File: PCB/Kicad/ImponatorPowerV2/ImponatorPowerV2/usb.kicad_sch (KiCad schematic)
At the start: 10 parts, among them J1 USB type-c, U10 AO3401A, U4 ACS37041

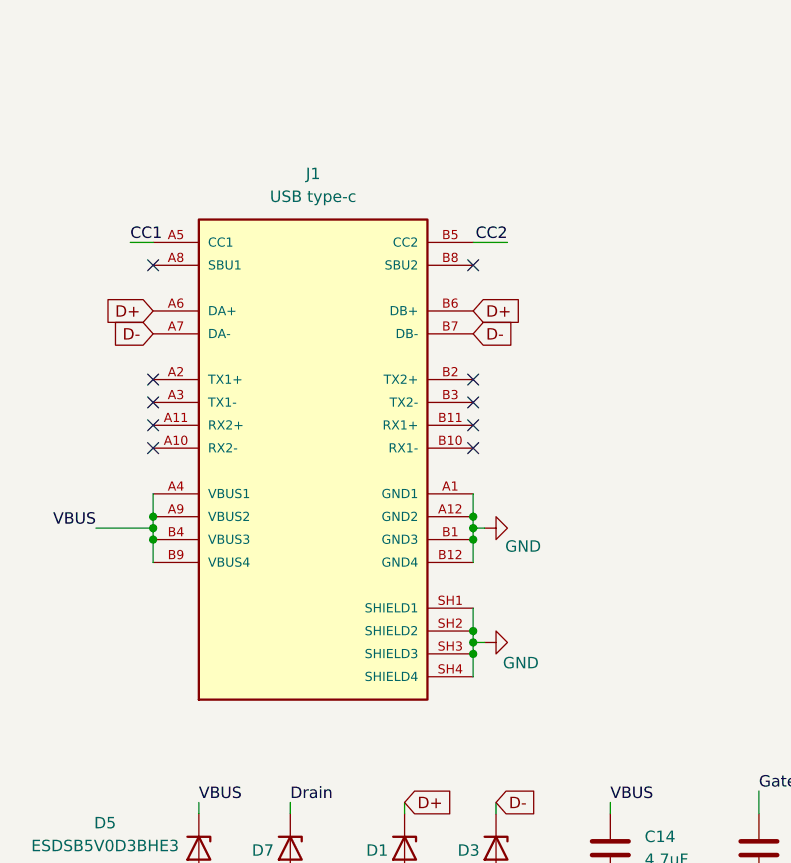
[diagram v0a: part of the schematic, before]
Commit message: PCB routed, not ready for production
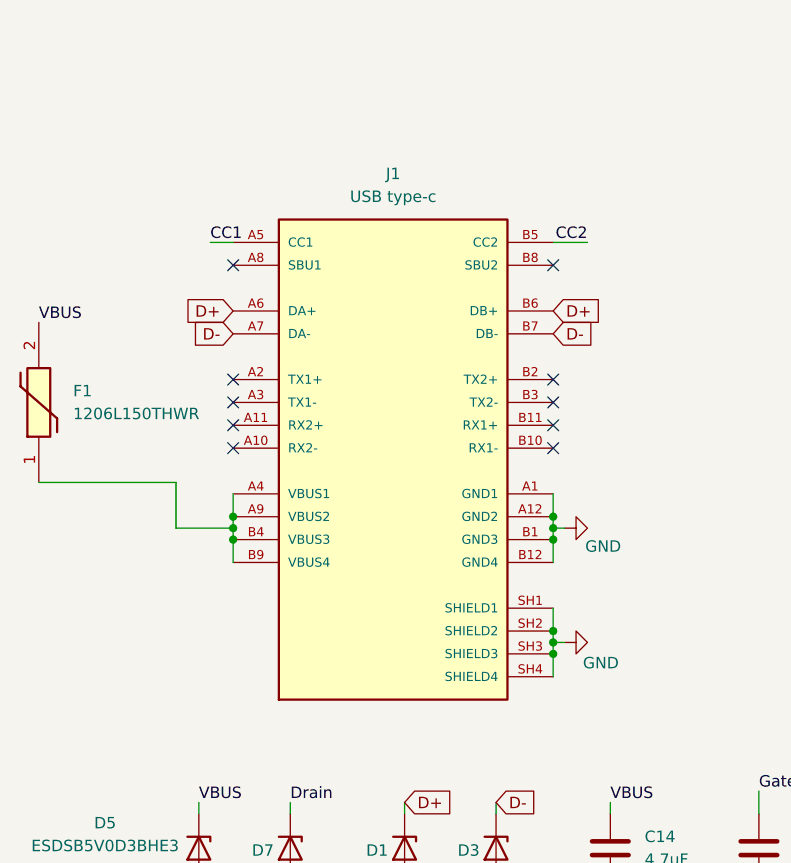
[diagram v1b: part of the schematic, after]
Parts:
- added F1: 1206L150THWR, custom2:FUSC3216X100N, symbol imported2:1206L150THWR
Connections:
- net VBUS: now also F1.2; no longer J1.A4 (VBUS1), J1.A9 (VBUS2), J1.B4 (VBUS3), J1.B9 (VBUS4)
- new net: F1.1, J1.A4 (VBUS1), J1.A9 (VBUS2), J1.B4 (VBUS3), J1.B9 (VBUS4)
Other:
- moved on the sheet: J1
